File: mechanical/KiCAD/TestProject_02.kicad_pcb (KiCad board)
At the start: 2 copper layers, 32 x 28 mm, 2 parts, among them U1 ESP32-C3-WROOM-02, U2 HUSB238_xxxDD

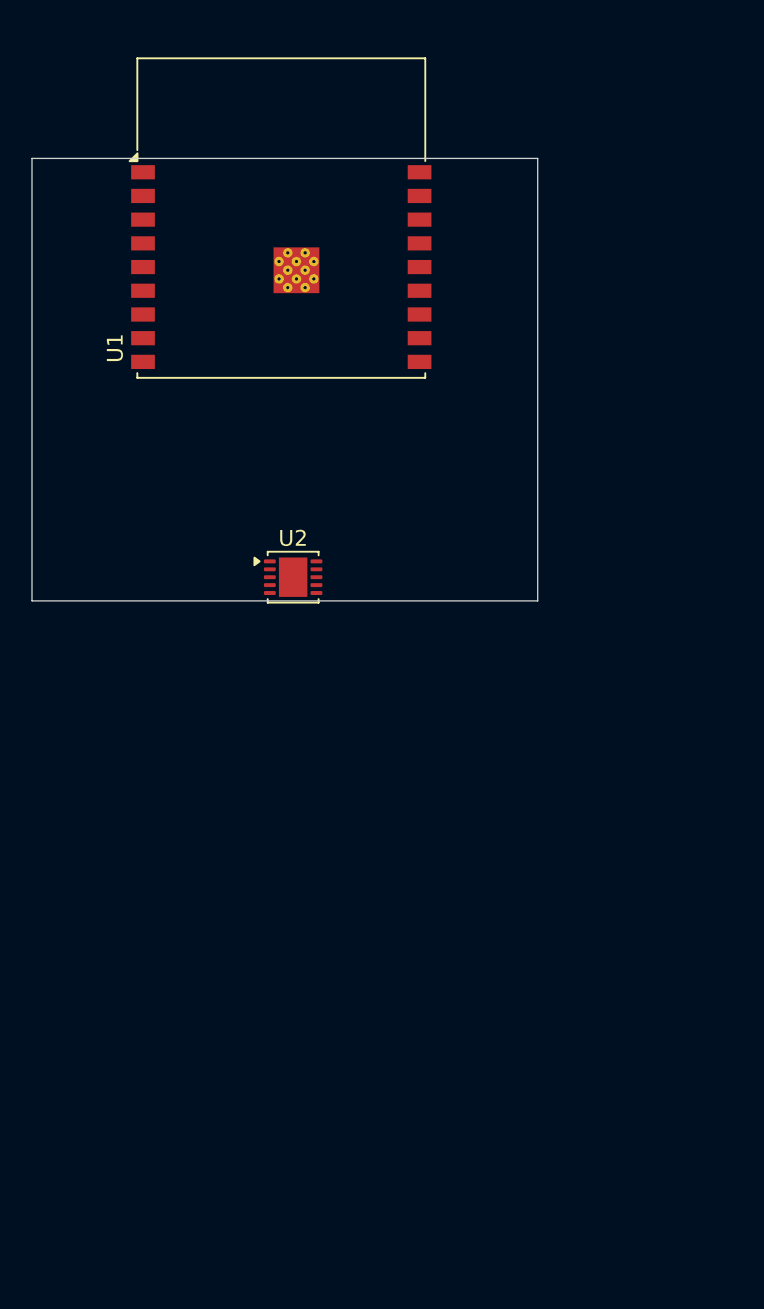
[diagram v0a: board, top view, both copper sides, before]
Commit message: Getting close to finishing the OBD PCB. Still needs some final touch ups, also some safety and reliability check.
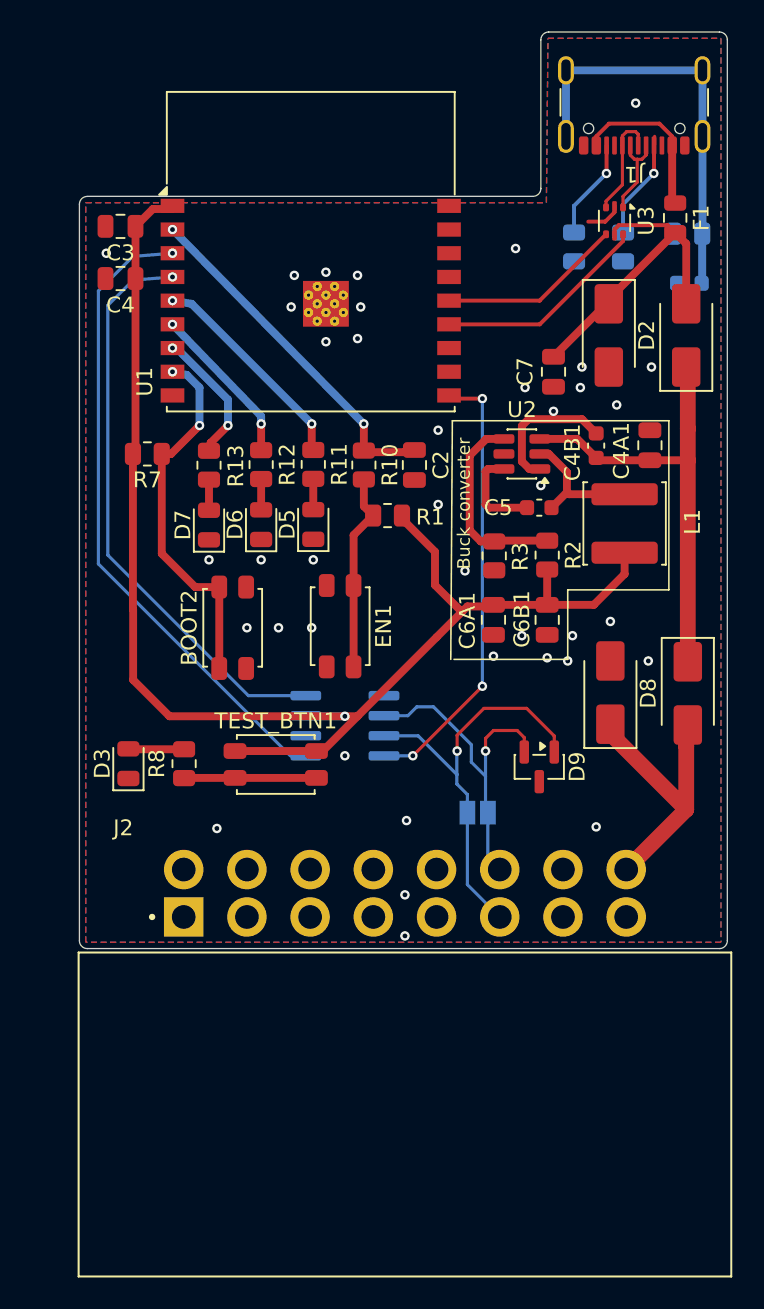
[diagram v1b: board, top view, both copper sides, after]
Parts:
- added BOOT2: SW_MEC_5E, Button_Switch_SMD:SW_SPST_EVQP2_MiddlePushTravel_H2.5mm, F.Cu at (55.7, 77.7)
- added C2: 0.1 uF, Capacitor_SMD:C_0805_2012Metric, F.Cu at (67.2, 67.4)
- added C3: 0.1 uF, Capacitor_SMD:C_0805_2012Metric, F.Cu at (48.6, 52.3)
- added C4: 100 nF, Capacitor_SMD:C_0805_2012Metric, F.Cu at (48.6, 55.6)
- added C4A1: 10uF, Capacitor_SMD:C_0805_2012Metric, F.Cu at (82.1, 66.2)
- added C4B1: 100nF, Capacitor_SMD:C_0603_1608Metric, F.Cu at (78.7, 66.2)
- added C5: 0.1 uF, Capacitor_SMD:C_0603_1608Metric, F.Cu at (75.1, 70.1)
- added C6A1: 22uF, Capacitor_SMD:C_0805_2012Metric, F.Cu at (72.2, 77.2)
- added C6B1: 22uF, Capacitor_SMD:C_0805_2012Metric, F.Cu at (75.6, 77.2)
- added C7: 10uF, Capacitor_SMD:C_0805_2012Metric, F.Cu at (76.0, 61.5)
- added C8: 4.7nF, Capacitor_SMD:C_0603_1608Metric, B.Cu at (84.6, 55.9)
- added D1: SMAJ5.0A, Diode_SMD:D_SMA, F.Cu at (79.5, 59.2)
- added D2: SS14, Diode_SMD:D_SMA, F.Cu at (84.4, 59.2)
- added D3: LED_G, LED_SMD:LED_0805_2012Metric, F.Cu at (49.1, 86.3)
- added D4: SMAJ24A, Diode_SMD:D_SMA, F.Cu at (79.6, 81.8)
- added D5: LED_G, LED_SMD:LED_0805_2012Metric, F.Cu at (60.8, 71.2)
- added D6: LED_B, LED_SMD:LED_0805_2012Metric, F.Cu at (57.5, 71.2)
- added D7: LED_R, LED_SMD:LED_0805_2012Metric, F.Cu at (54.2, 71.2)
- added D8: SS34, Diode_SMD:D_SMA, F.Cu at (84.5, 81.8)
- added D9: NUP2105L, Package_TO_SOT_SMD:SOT-23, F.Cu at (75.1, 86.5)
- added EN1: SW_MEC_5E, Button_Switch_SMD:SW_SPST_EVQP2_MiddlePushTravel_H2.5mm, F.Cu at (62.5, 77.6)
- added F1: Polyfuse, Fuse:Fuse_0805_2012Metric, F.Cu at (83.7, 51.8)
- added J1: USB_C_Receptacle_USB2.0_16P, Connector_USB:USB_C_Receptacle_GCT_USB4105-xx-A_16P_TopMnt_Horizontal, F.Cu at (81.1, 43.5)
- added J2: C-OBD-II-16M, C-OBD-II-16M:COMTECH_C-OBD-II-16M, F.Cu at (52.6, 96.0)
- added JP1: SolderJumper_2_Open, Jumper:SolderJumper-2_P1.3mm_Open_Pad1.0x1.5mm, B.Cu at (71.2, 89.4)
- added L1: 10uH, Inductor_SMD:L_Sunlord_SWPA5040S, F.Cu at (80.5, 71.1)
- added R1: 10k, Resistor_SMD:R_0805_2012Metric, F.Cu at (65.5, 70.6)
- added R10: 100R, Resistor_SMD:R_0805_2012Metric, F.Cu at (64.0, 67.4)
- added R11: 330R, Resistor_SMD:R_0805_2012Metric, F.Cu at (60.8, 67.4)
- added R12: 330R, Resistor_SMD:R_0805_2012Metric, F.Cu at (57.5, 67.4)
- added R13: 330R, Resistor_SMD:R_0805_2012Metric, F.Cu at (54.2, 67.4)
- added R2: 45.3K, Resistor_SMD:R_0805_2012Metric, F.Cu at (75.6, 73.1)
- added R3: 10k, Resistor_SMD:R_0805_2012Metric, F.Cu at (72.2, 73.2)
- added R4: 5.1K, Resistor_SMD:R_0805_2012Metric, B.Cu at (80.4, 53.6)
- added R5: 5.1K, Resistor_SMD:R_0805_2012Metric, B.Cu at (77.3, 53.6)
- added R6: 1M, Resistor_SMD:R_0805_2012Metric, B.Cu at (84.5, 52.8)
- added R7: 10k, Resistor_SMD:R_0805_2012Metric, F.Cu at (50.3, 66.7)
- added R8: 1.5K, Resistor_SMD:R_0805_2012Metric, F.Cu at (52.6, 86.3)
- added TEST_BTN1: SW_MEC_5E, Button_Switch_SMD:SW_SPST_EVQP2_MiddlePushTravel_H2.5mm, F.Cu at (58.4, 86.3)
- added U3: USBLC6-2P6, Package_TO_SOT_SMD:SOT-666, F.Cu at (79.9, 52.0)
- added U4: SN65HVD231, Package_SO:SOIC-8_3.9x4.9mm_P1.27mm, B.Cu at (62.8, 83.9)
- U2: value HUSB238_xxxDD -> TPS54302; footprint Package_DFN_QFN:WDFN-10-1EP_3x3mm_P0.5mm_EP1.8x2.5mm -> Package_TO_SOT_SMD:SOT-23-6
- moved U2 16.4 mm to (74.0, 66.7), turned to 180 degrees
- moved U1 2.83 mm to (60.6, 57.0)
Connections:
- U1 pad 1: unconnected-(U1-3V3-Pad1) -> +3.3V
- U1 pad 10: unconnected-(U1-IO10-Pad10) -> OPMODE
- U1 pad 13: unconnected-(U1-IO18-Pad13) -> USB_D-
- U1 pad 14: unconnected-(U1-IO19-Pad14) -> USB_D+
- U1 pad 19: Net-(U1-GND-Pad19) -> GND
- U1 pad 2: unconnected-(U1-EN-Pad2) -> EN
- U1 pad 3: unconnected-(U1-IO4-Pad3) -> CAN_TX
- U1 pad 4: unconnected-(U1-IO5-Pad4) -> CAN_RX
- U1 pad 5: unconnected-(U1-IO6-Pad5) -> Net-(U1-IO6)
- U1 pad 6: unconnected-(U1-IO7-Pad6) -> Net-(U1-IO7)
- U1 pad 7: unconnected-(U1-IO8-Pad7) -> Net-(U1-IO8)
- U1 pad 8: unconnected-(U1-IO9-Pad8) -> BOOT
- U1 pad 9: Net-(U1-GND-Pad19) -> GND
- U2 pad 1: unconnected-(U2-VIN-Pad1) -> GND
- U2 pad 2: unconnected-(U2-D+-Pad2) -> Net-(U2-SW)
- U2 pad 3: unconnected-(U2-D--Pad3) -> VIN
- U2 pad 4: unconnected-(U2-CC1-Pad4) -> Net-(U2-FB)
- U2 pad 6: unconnected-(U2-SDA-Pad6) -> Net-(U2-BOOT)
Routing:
- net +3.3V: track 0.00 -> 90.2 mm, vias 0 -> 1
- net CAN_TX: track 0.00 -> 40.3 mm, vias 0 -> 1
- net CAN_RX: track 0.00 -> 37.0 mm, vias 0 -> 1
- net VIN: track 0.00 -> 28.6 mm
- net OPMODE: track 0.00 -> 28.4 mm, vias 0 -> 3
- net CANH: track 0.00 -> 26.8 mm, vias 0 -> 1
- net Net-(J1-SHIELD): track 0.00 -> 26.6 mm
- net BOOT: track 0.00 -> 23.6 mm, vias 0 -> 2
- net EN: track 0.00 -> 22.2 mm, vias 0 -> 2
- net CANL: track 0.00 -> 21.8 mm, vias 0 -> 1
- net Net-(D1-A1): track 0.00 -> 20.4 mm
- net Net-(D4-A1): track 0.00 -> 18.2 mm
- net Net-(U1-IO6): track 0.00 -> 13.7 mm, vias 0 -> 2
- net USB_D-: track 0.00 -> 13.6 mm
- net Net-(EN1-Pad1): track 0.00 -> 12.6 mm
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- added copper zone on B.Cu, net GND
- added copper zone on F.Cu, net GND
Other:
- board size 32 x 28 mm -> 41 x 58 mm
- board text added: "Buck converter"

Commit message: Relocated buck converter and CAN transciever, added a mounting hole to secure the casing later.
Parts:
- added J3: TXD_PAD, TestPoint:TestPoint_Pad_2.0x2.0mm, B.Cu at (73.6, 60.4)
- added J4: RXD_PAD, TestPoint:TestPoint_Pad_2.0x2.0mm, B.Cu at (73.6, 56.0)
- added MountingHole: MountingHole_3.2mm_M3_Pad_Via, MountingHole:MountingHole_3.2mm_M3_Pad_Via, F.Cu at (77.5, 68.7)
- moved JP1 13.8 mm to (57.4, 88.4), turned to -90 degrees
- moved D9 11.6 mm to (63.9, 89.5), turned to 180 degrees
- moved U4 11.5 mm to (51.8, 80.6), turned to -90 degrees
- moved C4B1 9.46 mm to (76.1, 75.3)
- moved C5 9.46 mm to (72.5, 79.2)
- moved L1 9.46 mm to (77.9, 80.2)
- moved R2 9.46 mm to (73.0, 82.2)
- moved C6A1 9.46 mm to (69.6, 86.3)
- moved C4A1 9.46 mm to (79.5, 75.2)
- moved C6B1 9.46 mm to (73.0, 86.3)
- moved R3 9.46 mm to (69.7, 82.2)
- moved U2 9.46 mm to (71.4, 75.8)
- moved D4 5.53 mm to (78.4, 87.2), turned to 180 degrees
- moved C8 2.10 mm to (84.7, 53.8)
- moved R6 1.66 mm to (84.5, 51.1)
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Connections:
- U1 pad 11: unconnected-(U1-IO20/RXD-Pad11) -> Net-(J3-Pin_1)
- U1 pad 12: unconnected-(U1-IO21/TXD-Pad12) -> Net-(J4-Pin_1)
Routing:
- net CAN_TX: track 40.3 -> 25.9 mm
- net CAN_RX: track 37.0 -> 25.0 mm
- net CANL: track 21.8 -> 29.8 mm
- net OPMODE: track 28.4 -> 36.3 mm, vias 3 -> 1
- net Net-(J4-Pin_1): track 0.00 -> 6.98 mm, vias 0 -> 1
- net Net-(J3-Pin_1): track 0.00 -> 4.67 mm, vias 0 -> 1
- net +3.3V: track 90.2 -> 94.7 mm
- net CANH: track 26.8 -> 29.8 mm
- net VIN: track 28.6 -> 31.2 mm
- net Net-(D4-A1): track 18.2 -> 15.6 mm
- net Net-(J1-SHIELD): track 26.6 -> 24.6 mm
- net Net-(U1-IO7): track 10.2 -> 11.3 mm
- net Net-(U1-IO6): track 13.7 -> 14.5 mm
- net Net-(U1-IO8): track 8.56 -> 9.10 mm
- net Net-(U2-FB): track 12.6 -> 13.2 mm
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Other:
- board text added: "D1"
- board text added: "D2"
